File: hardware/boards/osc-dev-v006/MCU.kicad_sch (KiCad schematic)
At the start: 9 parts, among them J3 PIN-V, SW1 SW_Push, U3 CH32V006F8P6

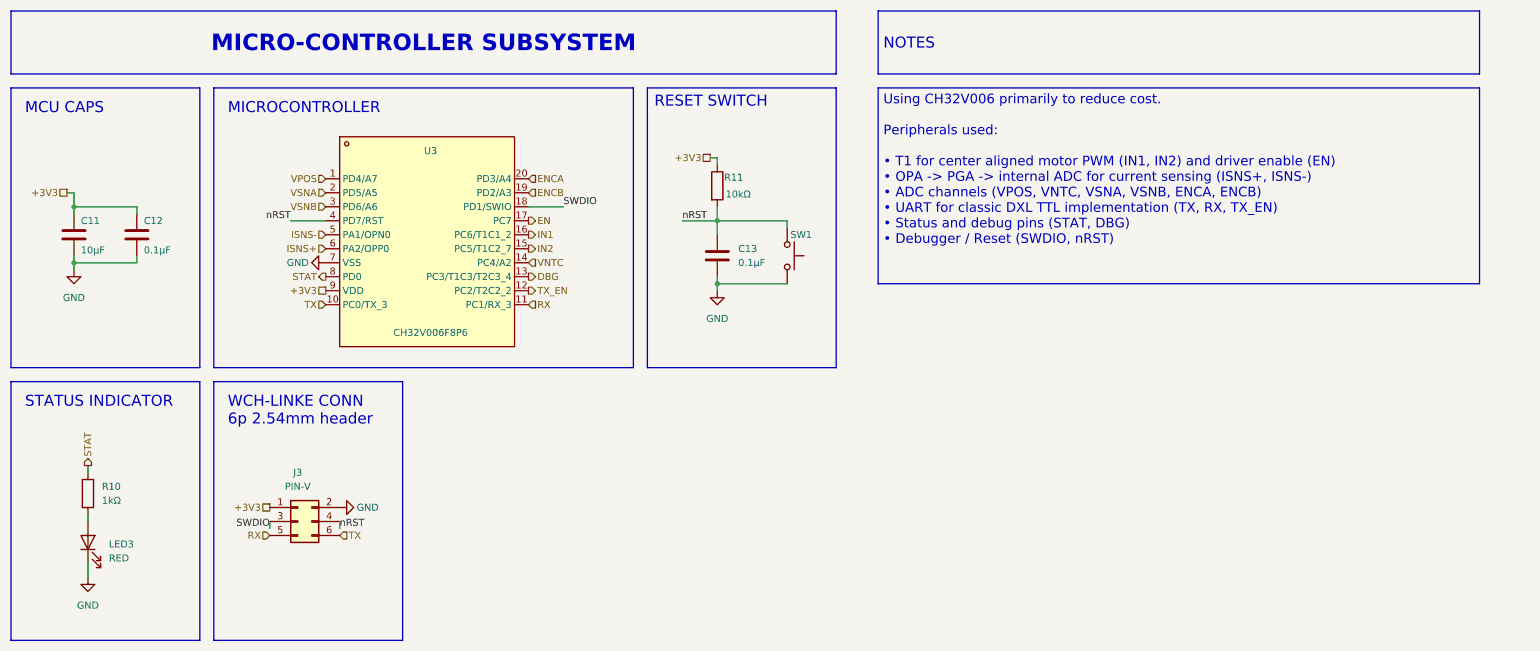
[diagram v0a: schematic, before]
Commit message: OSC DEV CH32 REV B (#10)
* update board

* updated schematics. ERC on schematics is now passing

* completed routing.

* adding ground vias

* update schematics notes

* update bom and component properties

* use red header pins for jumpers

* rename board to osc-dev-v006

* add docs
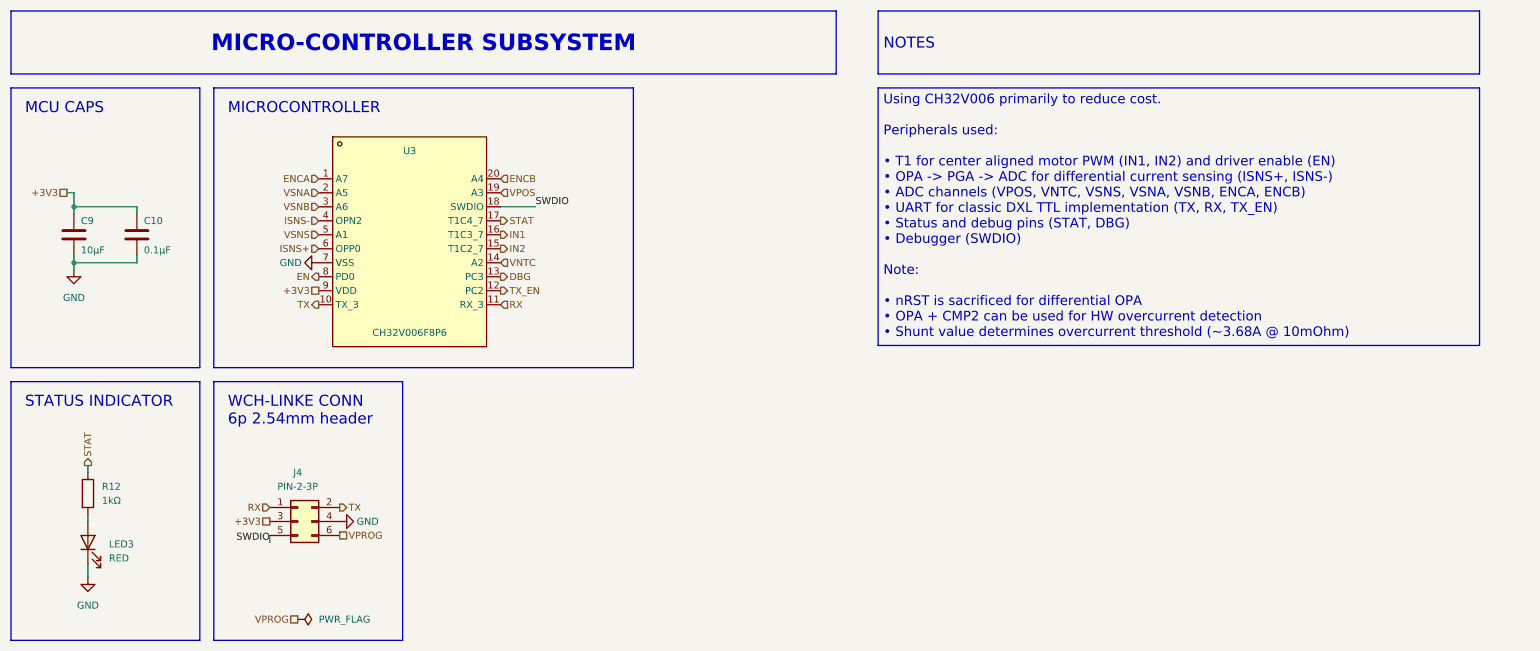
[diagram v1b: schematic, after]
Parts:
- removed C13: 0.1µF, Capacitor_SMD:C_0805_2012Metric_Pad1.18x1.45mm_HandSolder, symbol Device:C
- removed R11: 10kΩ, Resistor_SMD:R_0805_2012Metric_Pad1.20x1.40mm_HandSolder, symbol Device:R
- removed SW1: SW_Push, Button_Switch_SMD:SW_SPST_TS-1088-xR020, symbol Switch:SW_Push
- J4: renamed from J3; value PIN-V -> PIN-2-3P
- renumbered C12 to C10, C11 to C9, R10 to R12
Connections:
- net +3V3: now also J4.3 (Pin_3); no longer J4.1 (Pin_1)
- net EN: now also U3.8 (PD0); no longer U3.17 (PC7)
- net ENCA: now also U3.1 (PD4); no longer U3.20 (PD3/A4)
- net ENCB: now also U3.20 (PD3); no longer U3.19 (PD2/A3)
- net GND: now also J4.4 (Pin_4); no longer J4.2 (Pin_2)
- net ISNS-: now also U3.4 (PA4); no longer U3.5 (PA1/OPN0)
- net RX: now also J4.1 (Pin_1); no longer J4.5 (Pin_5)
- net STAT: now also U3.17 (PC7); no longer U3.8 (PD0)
- net SWDIO: now also J4.5 (Pin_5); no longer J4.3 (Pin_3)
- net TX: now also J4.2 (Pin_2); no longer J4.6 (Pin_6)
- net VPOS: now also U3.19 (PD2); no longer U3.1 (PD4/A7)
- removed net nRST: J4.4 (Pin_4), U3.4 (PD7/RST)
- new net VPROG: J4.6 (Pin_6)
- new net VSNS: U3.5 (PA1)
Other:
- note removed: "RESET SWITCH"
- moved on the sheet: U3

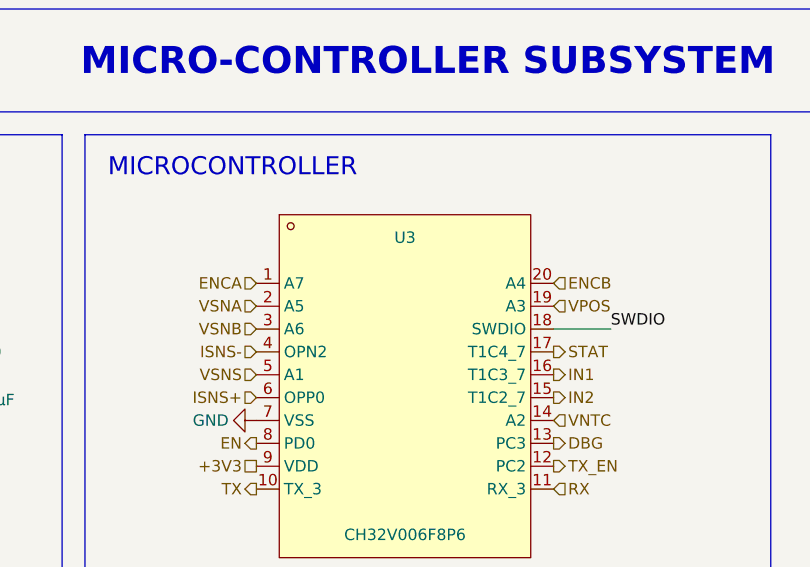
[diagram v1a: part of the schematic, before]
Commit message: final check and swapping ENCA/ENCB
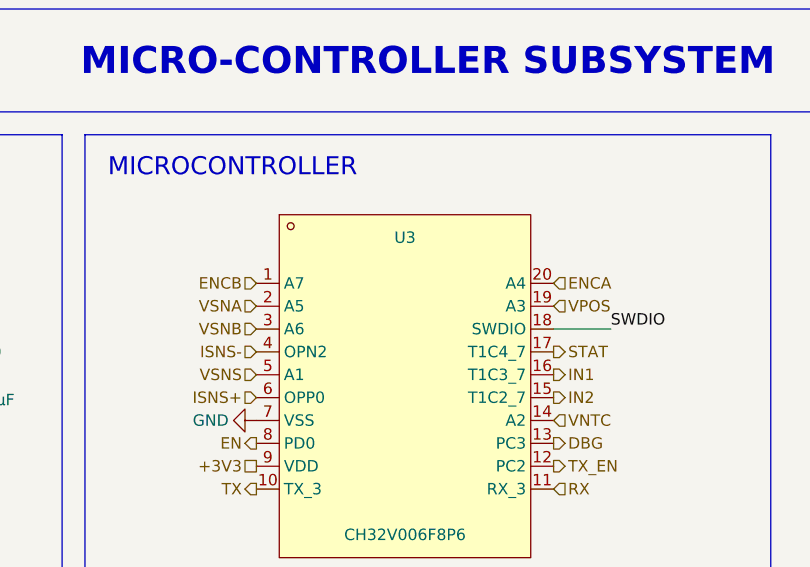
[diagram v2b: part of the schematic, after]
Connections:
- net ENCA: now also U3.20 (PD3); no longer U3.1 (PD4)
- net ENCB: now also U3.1 (PD4); no longer U3.20 (PD3)
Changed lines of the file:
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@@
+		)
+	)
+	(hierarchical_label "VSNB"
+		(shape input)
+		(at 71.12 50.8 180)
+		(effects
+			(font
+				(size 1.27 1.27)
+			)
+			(justify right)
+		)
+	)
+	(hierarchical_label "VPROG"
+		(shape passive)
+		(at 74.93 110.49 0)
+		(effects
+			(font
+				(size 1.27 1.27)
+			)
+			(justify left)
+		)
+	)
+	(hierarchical_label "RX"
+		(shape input)
+		(at 104.14 68.58 0)
+		(effects
+			(font
+				(size 1.27 1.27)
+			)
+			(justify left)
+		)
+	)
+	(hierarchical_label "STAT"
+		(shape output)
+		(at 29.21 97.79 90)
+		(effects
+			(font
+				(size 1.27 1.27)
+			)
+			(justify left)
 		)
 	)
 	(hierarchical_label "ENCA"
 		(shape input)
+		(at 104.14 45.72 0)
+		(effects
+			(font
+				(size 1.27 1.27)
+			)
+			(justify left)
+		)
+	)
+	(hierarchical_label "STAT"
+		(shape output)
+		(at 104.14 53.34 0)
+		(effects
+			(font
+				(size 1.27 1.27)
+			)
+			(justify left)
+		)
+	)
+	(hierarchical_label "IN2"
+		(shape output)
+		(at 104.14 58.42 0)
+		(effects
+			(font
+				(size 1.27 1.27)
+			)
+			(justify left)
+		)
+	)
+	(hierarchical_label "VPROG"
+		(shape passive)
+		(at 67.31 125.73 180)
+		(effects
+			(font
+				(size 1.27 1.27)
+			)
+			(justify right)
+		)
+	)
+	(hierarchical_label "EN"
+		(shape output)
+		(at 71.12 63.5 180)
+		(effects
+			(font
+				(size 1.27 1.27)
+			)
+			(justify right)
+		)
+	)
+	(hierarchical_label "ISNS+"
+		(shape input)
+		(at 71.12 58.42 180)
+		(effects
+			(font
+				(size 1.27 1.27)
+			)
+			(justify right)
+		)
+	)
+	(hierarchical_label "+3V3"
+		(shape passive)
+		(at 62.23 107.95 180)
+		(effects
+			(font
+				(size 1.27 1.27)
+			)
+			(justify right)
+		)
+	)
+	(hierarchical_label "VSNA"
+		(shape input)
+		(at 71.12 48.26 180)
+		(effects
+			(font
+				(size 1.27 1.27)
+			)
+			(justify right)
+		)
+	)
+	(hierarchical_label "ENCB"
+		(shape input)
 		(at 71.12 45.72 180)
 		(effects
@@
 		)
 	)
-	(hierarchical_label "VSNB"
-		(shape input)
-		(at 71.12 50.8 180)
-		(effects
-			(font
-				(size 1.27 1.27)
-			)
-			(justify right)
-		)
-	)
-	(hierarchical_label "VPROG"
-		(shape passive)
-		(at 74.93 110.49 0)
-		(effects
-			(font
-				(size 1.27 1.27)
-			)
-			(justify left)
-		)
-	)
 	(hierarchical_label "RX"
 		(shape input)
-		(at 104.14 68.58 0)
-		(effects
-			(font
-				(size 1.27 1.27)
-			)
-			(justify left)
-		)
-	)
-	(hierarchical_label "STAT"
-		(shape output)
-		(at 29.21 97.79 90)
-		(effects
-			(font
-				(size 1.27 1.27)
-			)
-			(justify left)
-		)
-	)
-	(hierarchical_label "STAT"
-		(shape output)
-		(at 104.14 53.34 0)
-		(effects
-			(font
-				(size 1.27 1.27)
-			)
-			(justify left)
-		)
-	)
-	(hierarchical_label "IN2"
-		(shape output)
-		(at 104.14 58.42 0)
-		(effects
-			(font
-				(size 1.27 1.27)
-			)
-			(justify left)
-		)
-	)
-	(hierarchical_label "VPROG"
-		(shape passive)
-		(at 67.31 125.73 180)
-		(effects
-			(font
-				(size 1.27 1.27)
-			)
-			(justify right)
-		)
-	)
-	(hierarchical_label "EN"
-		(shape output)
-		(at 71.12 63.5 180)
-		(effects
-			(font
-				(size 1.27 1.27)
-			)
-			(justify right)
-		)
-	)
-	(hierarchical_label "ISNS+"
-		(shape input)
-		(at 71.12 58.42 180)
+		(at 62.23 105.41 180)
 		(effects
 			(font
@@
 	(hierarchical_label "+3V3"
 		(shape passive)
-		(at 62.23 107.95 180)
-		(effects
-			(font
-				(size 1.27 1.27)
-			)
-			(justify right)
-		)
-	)
-	(hierarchical_label "VSNA"
-		(shape input)
-		(at 71.12 48.26 180)
-		(effects
-			(font
-				(size 1.27 1.27)
-			)
-			(justify right)
-		)
-	)
-	(hierarchical_label "RX"
-		(shape input)
-		(at 62.23 105.41 180)
-		(effects
-			(font
-				(size 1.27 1.27)
-			)
-			(justify right)
+		(at 25.4 48.26 180)
+		(effects
+			(font
+				(size 1.27 1.27)
+			)
+			(justify right)
+		)
+	)
+	(hierarchical_label "TX"
+		(shape output)
+		(at 71.12 68.58 180)
+		(effects
+			(font
+				(size 1.27 1.27)
+			)
+			(justify right)
+		)
+	)
+	(hierarchical_label "TX"
+		(shape output)
+		(at 74.93 105.41 0)
+		(effects
+			(font
+				(size 1.27 1.27)
+			)
+			(justify left)
 		)
 	)
 	(hierarchical_label "+3V3"
 		(shape passive)
-		(at 25.4 48.26 180)
-		(effects
-			(font
-				(size 1.27 1.27)
-			)
-			(justify right)
-		)
-	)
-	(hierarchical_label "TX"
-		(shape output)
-		(at 71.12 68.58 180)
-		(effects
-			(font
-				(size 1.27 1.27)
-			)
-			(justify right)
-		)
-	)
-	(hierarchical_label "TX"
-		(shape output)
-		(at 74.93 105.41 0)
-		(effects
-			(font
-				(size 1.27 1.27)
-			)
-			(justify left)
-		)
-	)
-	(hierarchical_label "+3V3"
-		(shape passive)
 		(at 71.12 66.04 180)
 		(effects
@@
 		(effects
 			(font
-				(size 1.27 1.27)
-			)
-			(justify left)
-		)
-	)
-	(hierarchical_label "ENCB"
-		(shape input)
-		(at 104.14 45.72 0)
-		(effects
-			(font

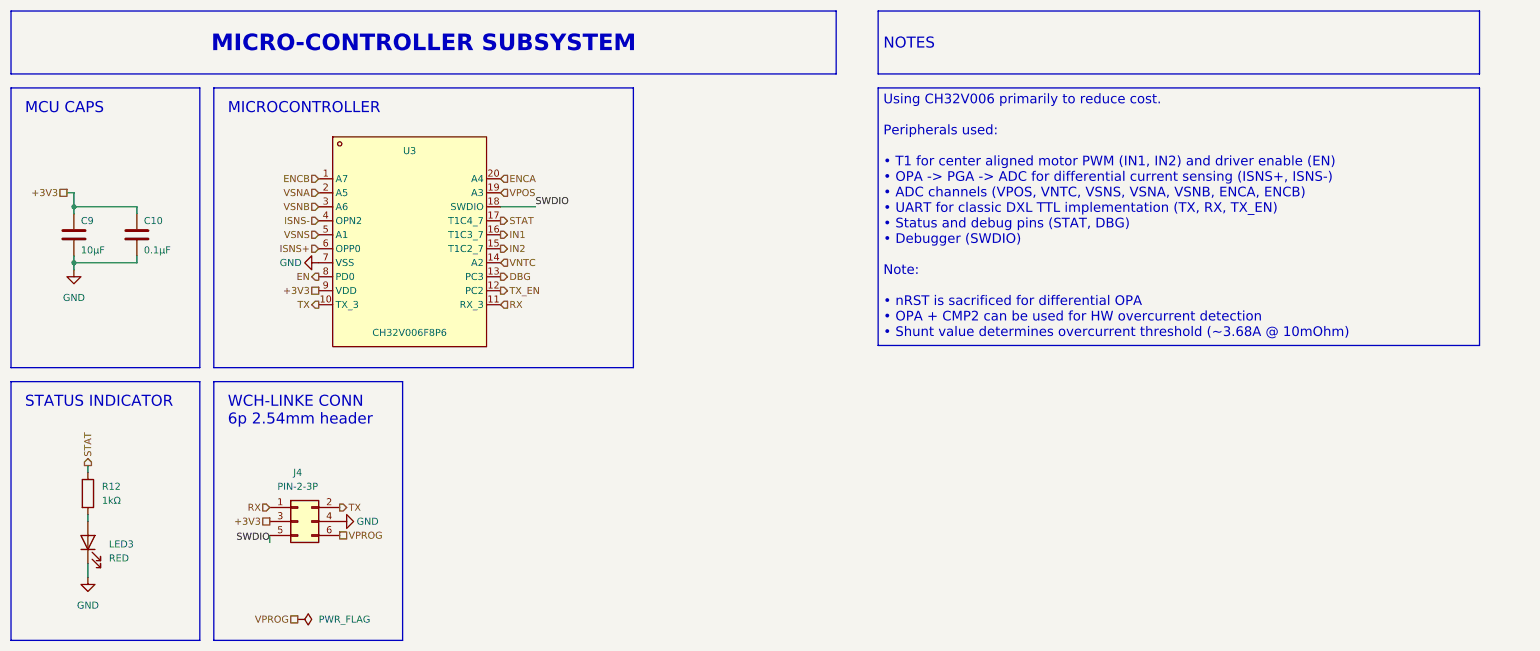
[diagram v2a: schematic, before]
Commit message: OSC Dev V006 Rev B patch (#21)
* osc-dev-v006: add SB1 bootstrap bridge for nRST/OPN

* osc-dev-v006: docs — Rev B validated, SB1 in-rev patch
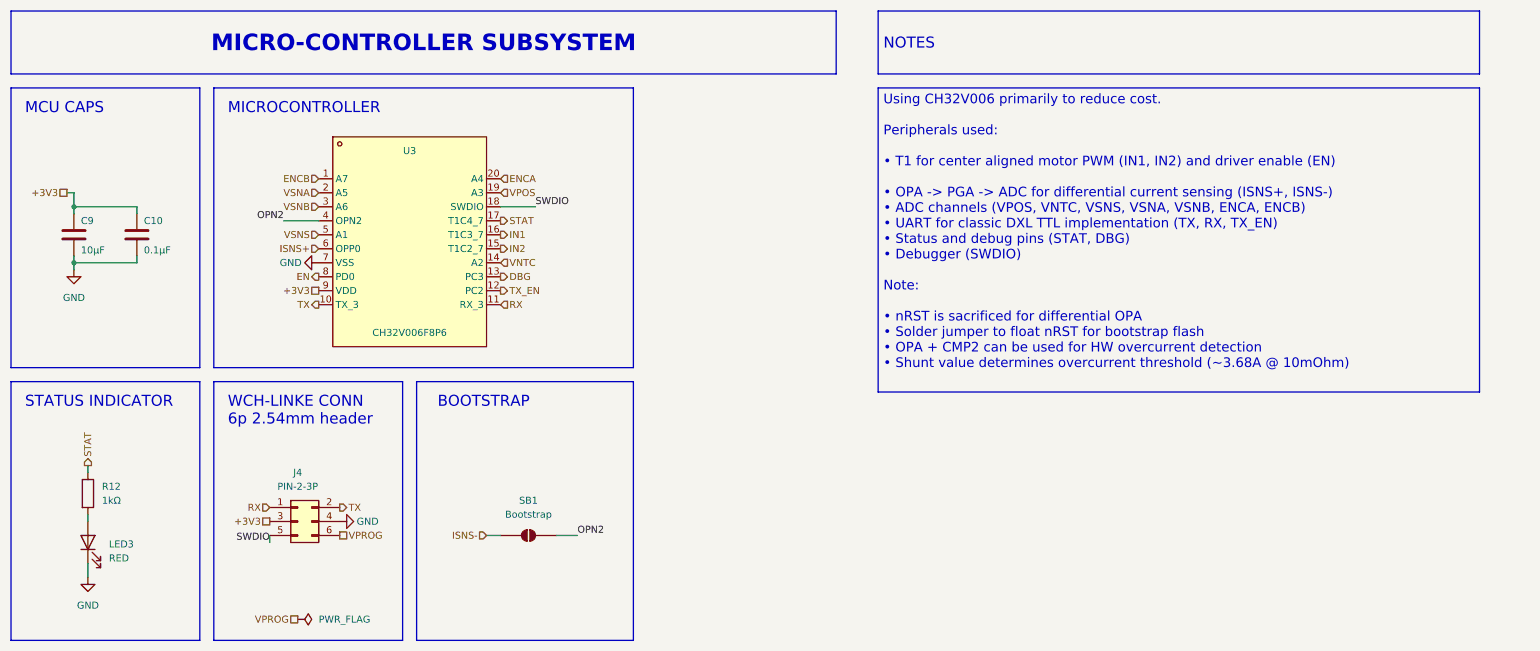
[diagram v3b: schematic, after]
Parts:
- added SB1: Bootstrap, Jumper:SolderJumper-2_P1.3mm_Open_RoundedPad1.0x1.5mm, symbol Jumper:SolderJumper_2_Open
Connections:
- net ISNS-: now also SB1.1 (A); no longer U3.4 (PA4)
- new net OPN2: SB1.2 (B), U3.4 (PA4)
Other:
- note added: "BOOTSTRAP"
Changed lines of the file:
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@@
+	)
+	(rectangle
+		(start 88.9 82.55)
+		(end 128.27 129.54)
+		(stroke
+			(width 0)
+			(type default)
+		)
+		(fill
+			(type none)
+		)
 	)
 	(rectangle
@@
 		)
 	)
+	(text "BOOTSTRAP"
+		(exclude_from_sim no)
+		(at 92.71 85.09 0)
+		(effects
+			(font
+				(size 2 2)
+				(thickness 0.25)
+			)
+			(justify left top)
+		)
+	)
 	(text "WCH-LINKE CONN\n6p 2.54mm header"
 		(exclude_from_sim no)
@@
 		)
 	)
-	(text_box "Using CH32V006 primarily to reduce cost.\n\nPeripherals used:\n\n  • T1 for center aligned motor PWM (IN1, IN2) and driver enable (EN)\n  • OPA -> PGA -> ADC for differential current sensing (ISNS+, ISNS-)\n  • ADC channels (VPOS, VNTC, VSNS, VSNA, VSNB, ENCA, ENCB)\n  • UART for classic DXL TTL implementation (TX, RX, TX_EN)\n  • Status and debug pins (STAT, DBG)\n  • Debugger (SWDIO)\n\nNote:\n\n  • nRST is sacrificed for differential OPA\n  • OPA + CMP2 can be used for HW overcurrent detection\n  • Shunt value determines overcurrent threshold (~3.68A @ 10mOhm)"
+	(text_box "Using CH32V006 primarily to reduce cost.\n\nPeripherals used:\n\n  • T1 for center aligned motor PWM (IN1, IN2) and driver enable (EN)\n\n  • OPA -> PGA -> ADC for differential current sensing (ISNS+, ISNS-)\n  • ADC channels (VPOS, VNTC, VSNS, VSNA, VSNB, ENCA, ENCB)\n  • UART for classic DXL TTL implementation (TX, RX, TX_EN)\n  • Status and debug pins (STAT, DBG)\n  • Debugger (SWDIO)\n\nNote:\n\n  • nRST is sacrificed for differential OPA\n  • Solder jumper to float nRST for bootstrap flash\n  • OPA + CMP2 can be used for HW overcurrent detection\n  • Shunt value determines overcurrent threshold (~3.68A @ 10mOhm)"
 		(exclude_from_sim no)
 		(at 172.72 29.21 0)
-		(size 109.22 46.7709)
+		(size 109.22 55.2231)
 		(margins 0.9525 0.9525 0.9525 0.9525)
 		(stroke
@@
 	(wire
 		(pts
+			(xy 101.6 110.49) (xy 104.14 110.49)
+		)
+		(stroke
+			(width 0)
+			(type default)
+		)
+	)
+	(wire
+		(pts
 			(xy 26.67 60.96) (xy 26.67 62.23)
 		)
@@
 		(pts
 			(xy 38.1 50.8) (xy 38.1 52.07)
+		)
+		(stroke
+			(width 0)
+			(type default)
+		)
+	)
+	(wire
+		(pts
+			(xy 64.77 53.34) (xy 71.12 53.34)
+		)
+		(stroke
+			(width 0)
+			(type default)
+		)
+	)
+	(wire
+		(pts
+			(xy 118.11 110.49) (xy 114.3 110.49)
 		)
 		(stroke
@@
 	(label "SWDIO"
 		(at 110.49 50.8 0)
+		(effects
+			(font
+				(size 1.27 1.27)
+			)
+			(justify left bottom)
+		)
+	)
+	(label "OPN2"
+		(at 64.77 53.34 180)
+		(effects
+			(font
+				(size 1.27 1.27)
+			)
+			(justify right bottom)
+		)
+	)
+	(label "OPN2"
+		(at 118.11 110.49 0)
 		(effects
 			(font
@@
 	(hierarchical_label "ISNS-"
 		(shape input)
-		(at 71.12 53.34 180)
+		(at 101.6 110.49 180)
 		(effects
 			(font
@@
 					(unit 1)
 				)
+			)
+		)
+	)
+	(symbol
+		(lib_id "Jumper:SolderJumper_2_Open")
+		(at 109.22 110.49 0)
+		(unit 1)
+		(body_style 1)
+		(exclude_from_sim no)
+		(in_bom no)
+		(on_board yes)
+		(in_pos_files yes)
+		(dnp no)
+		(fields_autoplaced yes)
+		(property "Reference" "SB1"
+			(at 109.22 104.14 0)
+			(show_name no)
+			(do_not_autoplace no)
+			(effects
+				(font
+					(size 1.27 1.27)
+				)
+			)
+		)
+		(property "Value" "Bootstrap"
+			(at 109.22 106.68 0)
+			(show_name no)
+			(do_not_autoplace no)
+			(effects
+				(font
+					(size 1.27 1.27)
+				)
+			)
+		)
+		(property "Footprint" "Jumper:SolderJumper-2_P1.3mm_Open_RoundedPad1.0x1.5mm"
+			(at 109.22 110.49 0)
+			(hide yes)
+			(show_name no)
+			(do_not_autoplace no)
+			(effects
+				(font
+					(size 1.27 1.27)
+				)
+			)
+		)
+		(property "Datasheet" ""
+			(at 109.22 118.11 0)
+			(hide yes)
+			(show_name no)
+			(do_not_autoplace no)
+			(effects
+				(font
+					(size 1.27 1.27)
+				)
+			)
+		)
+		(property "Description" "Solder Jumper, 2-pole, open"
+			(at 109.22 115.57 0)
+			(hide yes)
+			(show_name no)
+			(do_not_autoplace no)
+			(effects
+				(font
+					(size 1.27 1.27)
+				)
+			)
+		)
+		(pin "1"
+		)
+		(pin "2"
+		)
+		(instances
+			(project "osc-dev-v006"
+				(path "/6062e7d2-0c72-467e-b49c-6387ba053e09/77d3819f-1672-490a-859c-8df54ad0ab77"
+					(reference "SB1")
+					(unit 1)
+				)
